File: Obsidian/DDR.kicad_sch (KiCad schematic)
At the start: 59 parts, among them U2 MT41K512M16HA-125_E / MT41K51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

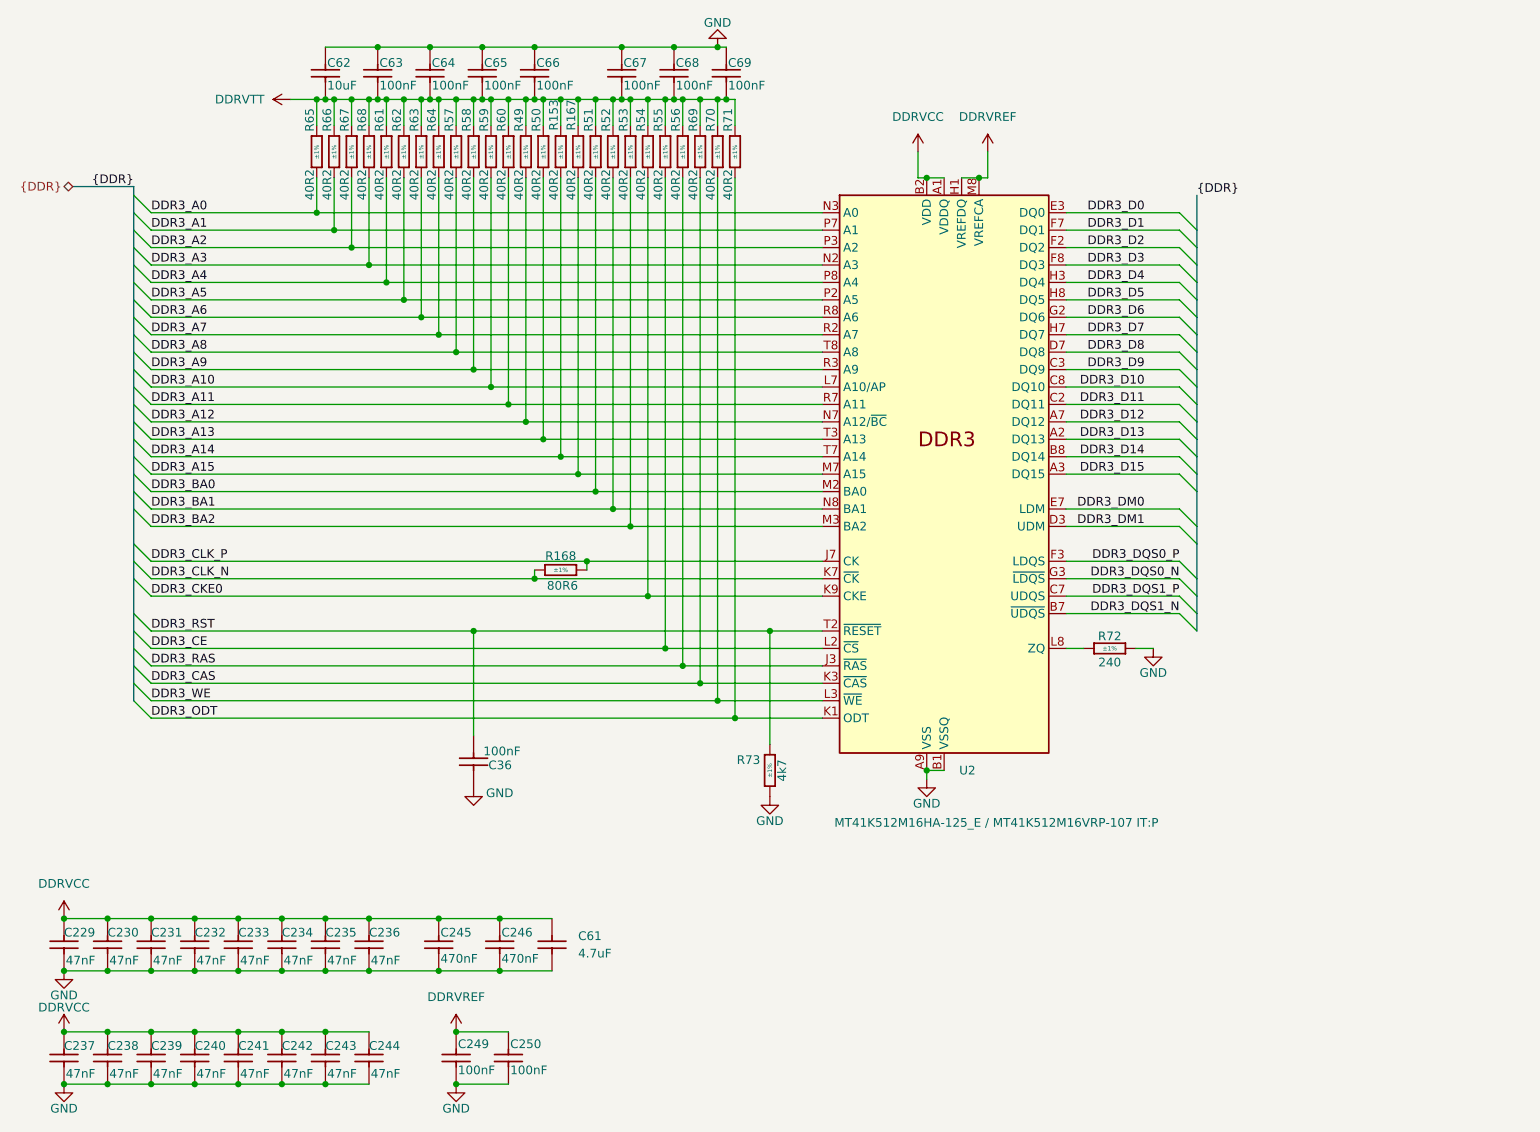
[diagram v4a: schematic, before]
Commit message: Cleaning symbol fields
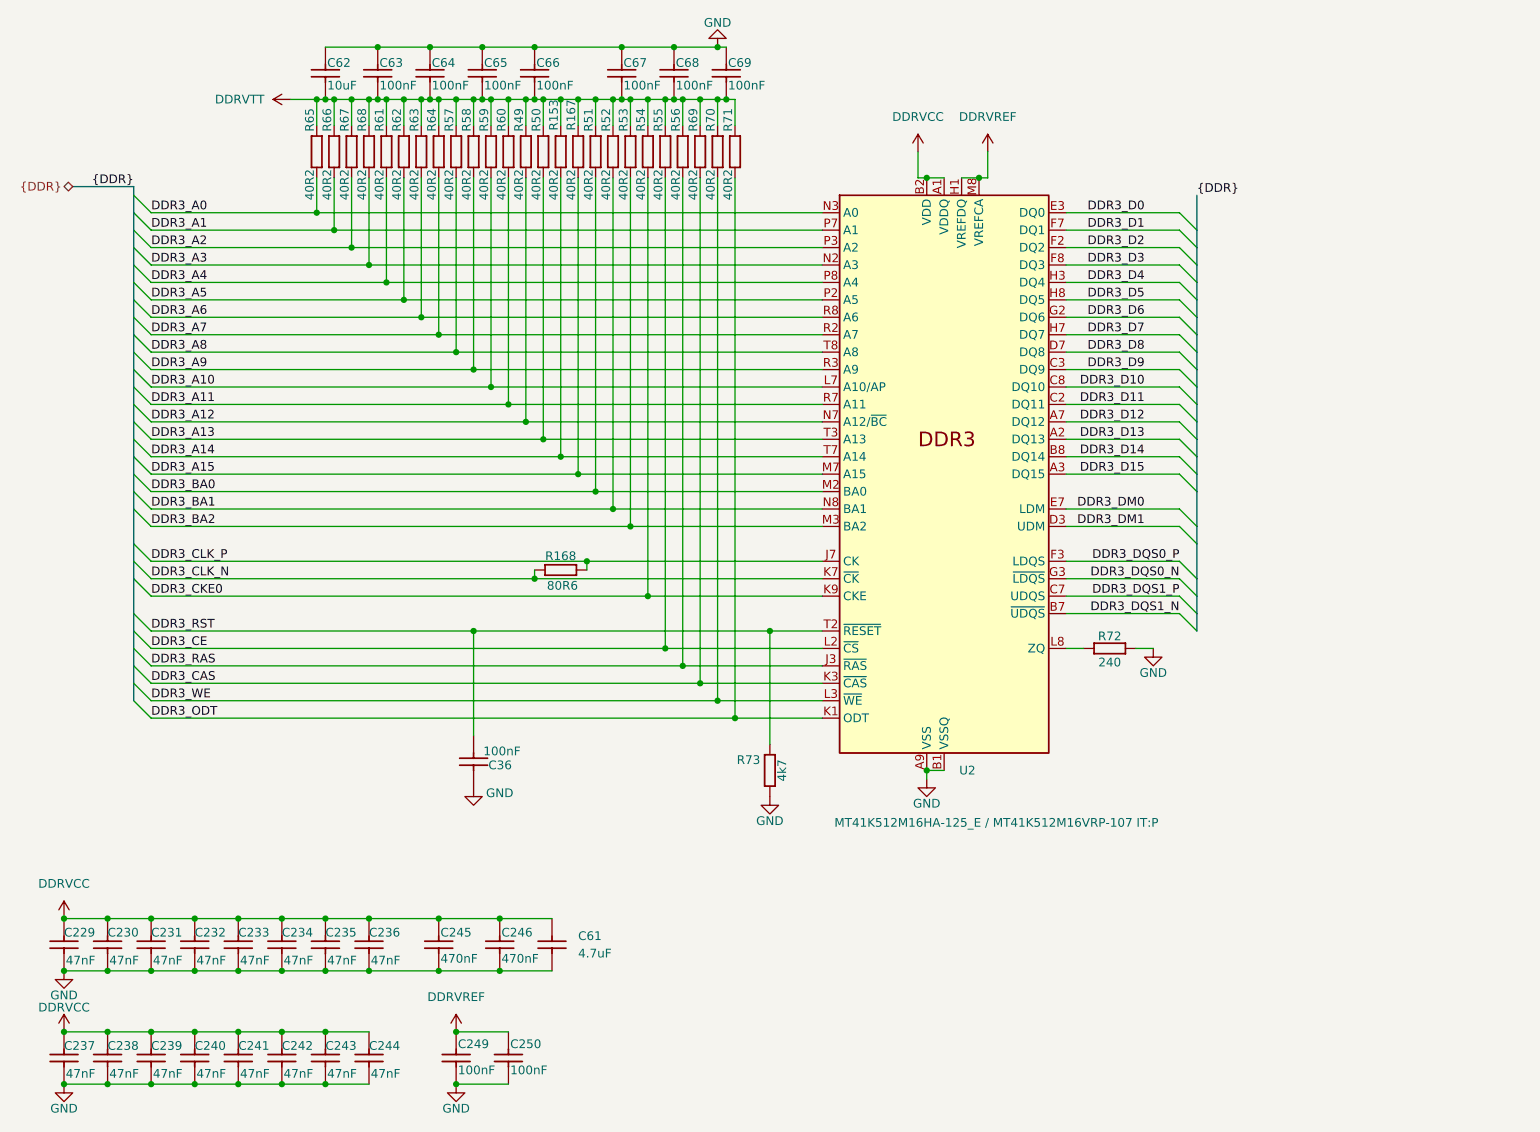
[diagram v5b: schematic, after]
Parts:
- C229, C230, C231, C232, C233, C234, C235, C236, C237, C238, C239, C240, C241, C242, C243, C244: Author CERN DEM JLC -> (none); Case 0201 -> (none); Comment 47nF -> (none); Component Kind Standard -> (none); Component Type Standard -> (none); ComponentHeight (none) -> (none); CreateDate 12/03/07 00:00:00 -> (none); Database Table Name Capacitors -> (none); Footprint Library Capacitors SMD -> (none); Footprint Path PcbLib\Capacitors SMD.PcbLib -> (none); Footprint Ref CAPC0603X33N -> (none); HelpURL \\cern.ch\dfs\Applications\Altium\Datasheets\CC0201_X5R_AVX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 -> (none); LatestRevisionDate 12/03/07 00:00:00 -> (none); Library Name Capacitors SMD -> (none); Library Path SchLib\Capacitors.SchLib -> (none); Library Ref Capacitor - non polarized -> (none); License CC-BY-SA 4.0 -> (none); Manufacturer GENERIC -> (none); Manufacturer Part Number CC0201_47NF_6.3V_10%_X5R -> (none); Manufacturer1 ComponentHeight 0.33mm -> (none); Manufacturer1 Example AVX -> (none); Manufacturer1 Part Number 02016D473KAT2A -> (none); Mounted Yes -> (none); PackageDescription (none) -> (none); Part Description SMD Multilayer Chip Ceramic Capacitor -> (none); Part Number CC0201_47NF_6.3V_10%_X5R -> (none); Pin Count 2 -> (none); PressFit (none) -> (none); SMD Yes -> (none); Sense No -> (none); Sense Comment (none) -> (none); Socket No -> (none); Status Not Recommended -> (none); Status Comment (none) -> (none); TC X5R -> (none); Tolerance ±10% -> (none); Voltage 6.3V -> (none)
- C245, C246: Author CERN DEM JLC -> (none); Case 0201 -> (none); Comment 470nF -> (none); Component Kind Standard -> (none); Component Type Standard -> (none); ComponentHeight (none) -> (none); CreateDate 05/27/10 00:00:00 -> (none); Database Table Name Capacitors -> (none); Footprint Library Capacitors SMD -> (none); Footprint Path PcbLib\Capacitors SMD.PcbLib -> (none); Footprint Ref CAPC0603X33N -> (none); HelpURL \\cern.ch\dfs\Applications\Altium\Datasheets\CC0201_X5R_TAI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 -> (none); LatestRevisionDate 05/27/10 00:00:00 -> (none); Library Name Capacitors SMD -> (none); Library Path SchLib\Capacitors.SchLib -> (none); Library Ref Capacitor - non polarized -> (none); License CC-BY-SA 4.0 -> (none); Manufacturer GENERIC -> (none); Manufacturer Part Number CC0201_470NF_4V_20%_X5R -> (none); Manufacturer1 ComponentHeight 0.33mm -> (none); Manufacturer1 Example TAIYO YUDEN -> (none); Manufacturer1 Part Number AMK063BJ474MP-F -> (none); Mounted Yes -> (none); PackageDescription (none) -> (none); Part Description SMD Multilayer Chip Ceramic Capacitor -> (none); Part Number CC0201_470NF_4V_20%_X5R -> (none); Pin Count 2 -> (none); PressFit (none) -> (none); SMD Yes -> (none); Sense No -> (none); Sense Comment (none) -> (none); Socket No -> (none); Status Not Recommended -> (none); Status Comment (none) -> (none); TC X5R -> (none); Tolerance ±20% -> (none); Voltage 4V -> (none)
- C249, C250: Author CERN DEM JLC -> (none); Case 0201 -> (none); Comment 100nF -> (none); Component Kind Standard -> (none); Component Type Standard -> (none); ComponentHeight (none) -> (none); CreateDate 12/03/07 00:00:00 -> (none); Database Table Name Capacitors -> (none); Footprint Library Capacitors SMD -> (none); Footprint Path PcbLib\Capacitors SMD.PcbLib -> (none); Footprint Ref CAPC0603X33N -> (none); HelpURL \\cern.ch\dfs\Applications\Altium\Datasheets\CC0201_X5R_AVX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 -> (none); LatestRevisionDate 12/03/07 00:00:00 -> (none); Library Name Capacitors SMD -> (none); Library Path SchLib\Capacitors.SchLib -> (none); Library Ref Capacitor - non polarized -> (none); License CC-BY-SA 4.0 -> (none); Manufacturer GENERIC -> (none); Manufacturer Part Number CC0201_100NF_6.3V_10%_X5R -> (none); Manufacturer1 ComponentHeight 0.33mm -> (none); Manufacturer1 Example AVX -> (none); Manufacturer1 Part Number 02016D104KAT2A -> (none); Mounted Yes -> (none); PackageDescription (none) -> (none); Part Description SMD Multilayer Chip Ceramic Capacitor -> (none); Part Number CC0201_100NF_6.3V_10%_X5R -> (none); Pin Count 2 -> (none); PressFit (none) -> (none); SMD Yes -> (none); Sense No -> (none); Sense Comment (none) -> (none); Socket No -> (none); Status Not Recommended -> (none); Status Comment (none) -> (none); TC X5R -> (none); Tolerance ±10% -> (none); Voltage 6.3V -> (none)
- C36, C63, C64, C65, C66, C67, C68, C69: Author CERN DEM MR -> (none); Case 0402 -> (none); Comment 100nF -> (none); Component Kind Standard -> (none); Component Type Standard -> (none); ComponentHeight (none) -> (none); CreateDate 06/30/17 00:00:00 -> (none); Database Table Name Capacitors -> (none); Footprint Library Capacitors SMD -> (none); Footprint Path PcbLib\Capacitors SMD.PcbLib -> (none); Footprint Ref CAPC1005X55N -> (none); HelpURL \\cern.ch\dfs\Applications\Altium\Datasheets\CC0402_MURATA_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 -> (none); LatestRevisionDate 06/30/17 00:00:00 -> (none); Library Name Capacitors SMD -> (none); Library Path SchLib\Capacitors.SchLib -> (none); Library Ref Capacitor - non polarized -> (none); License CC-BY-SA 4.0 -> (none); Manufacturer GENERIC -> (none); Manufacturer Part Number CC0402_100NF_50V_10%_X7R -> (none); Manufacturer1 ComponentHeight 0.55mm -> (none); Manufacturer1 Example MURATA -> (none); Manufacturer1 Part Number GRM155R71H104KE14D -> (none); Mounted Yes -> (none); PackageDescription (none) -> (none); Part Description SMD Multilayer Chip Ceramic Capacitor -> (none); Part Number CC0402_100NF_50V_10%_X7R -> (none); Pin Count 2 -> (none); PressFit (none) -> (none); SMD Yes -> (none); Sense No -> (none); Sense Comment (none) -> (none); Socket No -> (none); Status None -> (none); Status Comment (none) -> (none); TC X7R -> (none); Tolerance ±10% -> (none); Voltage 50V -> (none)
- C61: Author CERN DEM BC -> (none); Case 0402 -> (none); Comment 4.7uF -> (none); Component Kind Standard -> (none); Component Type Standard -> (none); ComponentHeight (none) -> (none); CreateDate 09/07/20 00:00:00 -> (none); Database Table Name Capacitors -> (none); Footprint Library Capacitors SMD -> (none); Footprint Path PcbLib\Capacitors SMD.PcbLib -> (none); Footprint Ref CAPC1005X55N -> (none); HelpURL \\cern.ch\dfs\Applications\Altium\Datasheets\CC0402_X5R_YAG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 -> (none); LatestRevisionDate 09/07/20 00:00:00 -> (none); Library Name Capacitors SMD -> (none); Library Path SchLib\Capacitors.SchLib -> (none); Library Ref Capacitor - non polarized -> (none); License CC-BY-SA 4.0 -> (none); Manufacturer GENERIC -> (none); Manufacturer Part Number CC0402_4.7UF_16V_20%_X5R -> (none); Manufacturer1 ComponentHeight 0.55mm -> (none); Manufacturer1 Example YAGEO PHYCOMP -> (none); Manufacturer1 Part Number CC0402MRX5R7BB475 -> (none); Mounted Yes -> (none); PackageDescription (none) -> (none); Part Description SMD Multilayer Chip Ceramic Capacitor -> (none); Part Number CC0402_4.7UF_16V_20%_X5R -> (none); Pin Count 2 -> (none); PressFit (none) -> (none); SMD Yes -> (none); Sense No -> (none); Sense Comment (none) -> (none); Socket No -> (none); Status Preferred -> (none); Status Comment (none) -> (none); TC X5R -> (none); Tolerance ±20% -> (none); Voltage 16V -> (none)
- C62: Author CERN DEM JLC -> (none); Case 0402 -> (none); Comment 10uF -> (none); Component Kind Standard -> (none); Component Type Standard -> (none); ComponentHeight (none) -> (none); CreateDate 01/07/15 00:00:00 -> (none); Database Table Name Capacitors -> (none); Footprint Library Capacitors SMD -> (none); Footprint Path PcbLib\Capacitors SMD.PcbLib -> (none); Footprint Ref CAPC1005X70N -> (none); HelpURL \\cern.ch\dfs\Applications\Altium\Datasheets\CC0402_X5R_TDK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 -> (none); LatestRevisionDate 01/07/15 00:00:00 -> (none); Library Name Capacitors SMD -> (none); Library Path SchLib\Capacitors.SchLib -> (none); Library Ref Capacitor - non polarized -> (none); License CC-BY-SA 4.0 -> (none); Manufacturer GENERIC -> (none); Manufacturer Part Number CC0402_10UF_6.3V_20%_X5R -> (none); Manufacturer1 ComponentHeight 0.70mm -> (none); Manufacturer1 Example TDK -> (none); Manufacturer1 Part Number C1005X5R0J106M050 -> (none); Mounted Yes -> (none); PackageDescription (none) -> (none); Part Description SMD Multilayer Chip Ceramic Capacitor -> (none); Part Number CC0402_10UF_6.3V_20%_X5R -> (none); Pin Count 2 -> (none); PressFit (none) -> (none); SMD Yes -> (none); Sense No -> (none); Sense Comment (none) -> (none); Socket No -> (none); Status Preferred -> (none); Status Comment (none) -> (none); TC X5R -> (none); Tolerance ±10% -> (none); Voltage 6.3V -> (none)
- R153, R167, R49, R50, R51, R52, R53, R54, R55, R56, R57, R58, R59, R60, R61, R62, R63, R64, R65, R66, R67, R68, R69, R70, R71: Author CERN DEM JLC -> (none); Case 0402 -> (none); Comment 40R2 -> (none); Component Kind Standard -> (none); Component Type Standard -> (none); ComponentHeight (none) -> (none); CreateDate 02/03/15 00:00:00 -> (none); Database Table Name Resistors -> (none); Footprint Library Resistors SMD -> (none); Footprint Path PcbLib\Resistors SMD.PcbLib -> (none); Footprint Ref RESC1005X40N -> (none); HelpURL \\cern.ch\dfs\Applications\Altium\Datasheets\R0402_VISHAY_C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 -> (none); LatestRevisionDate 02/03/15 00:00:00 -> (none); Library Name Resistors SMD -> (none); Library Path SchLib\Resistors.SchLib -> (none); Library Ref Resistor - 1% -> (none); License CC-BY-SA 4.0 -> (none); Manufacturer GENERIC -> (none); Manufacturer Part Number R0402_40R2_1%_0.0625W_100PPM -> (none); Manufacturer1 ComponentHeight 0.4mm -> (none); Manufacturer1 Example VISHAY -> (none); Manufacturer1 Part Number CRCW040240R2FK -> (none); Mounted Yes -> (none); PackageDescription (none) -> (none); Part Description General Purpose Thick Film Chip Resistor -> (none); Part Number R0402_40R2_1%_0.0625W_100PPM -> (none); Pin Count 2 -> (none); Power 0.0625W -> (none); PressFit No -> (none); SMD Yes -> (none); Sense No -> (none); Sense Comment (none) -> (none); Socket No -> (none); Status None -> (none); Status Comment (none) -> (none); TC ±100ppm/°C -> (none); Tolerance ±1% -> (none); Voltage (none) -> (none)
- R168: Author CERN DEM JLC -> (none); Case 0402 -> (none); Comment 80R6 -> (none); Component Kind Standard -> (none); Component Type Standard -> (none); ComponentHeight (none) -> (none); CreateDate 03/03/15 00:00:00 -> (none); Database Table Name Resistors -> (none); Footprint Library Resistors SMD -> (none); Footprint Path PcbLib\Resistors SMD.PcbLib -> (none); Footprint Ref RESC1005X40N -> (none); HelpURL \\cern.ch\dfs\Applications\Altium\Datasheets\R0402_PANASONI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 -> (none); LatestRevisionDate 03/03/15 00:00:00 -> (none); Library Name Resistors SMD -> (none); Library Path SchLib\Resistors.SchLib -> (none); Library Ref Resistor - 1% -> (none); License CC-BY-SA 4.0 -> (none); Manufacturer GENERIC -> (none); Manufacturer Part Number R0402_80R6_1%_0.1W_100PPM -> (none); Manufacturer1 ComponentHeight 0.4mm -> (none); Manufacturer1 Example PANASONIC -> (none); Manufacturer1 Part Number ERJ2RKF80R6X -> (none); Mounted Yes -> (none); PackageDescription (none) -> (none); Part Description General Purpose Thick Film Chip Resistor -> (none); Part Number R0402_80R6_1%_0.1W_100PPM -> (none); Pin Count 2 -> (none); Power 0.1W -> (none); PressFit No -> (none); SMD Yes -> (none); Sense No -> (none); Sense Comment (none) -> (none); Socket No -> (none); Status Not Recommended -> (none); Status Comment (none) -> (none); TC ±100ppm/°C -> (none); Tolerance ±1% -> (none); Voltage 50V -> (none)
- R72: Author CERN DEM JLC -> (none); Case 0402 -> (none); Comment 240 -> (none); Component Kind Standard -> (none); Component Type Standard -> (none); ComponentHeight (none) -> (none); CreateDate 12/03/07 00:00:00 -> (none); Database Table Name Resistors -> (none); Footprint Library Resistors SMD -> (none); Footprint Path PcbLib\Resistors SMD.PcbLib -> (none); Footprint Ref RESC1005X40N -> (none); HelpURL \\cern.ch\dfs\Applications\Altium\Datasheets\R0402_Phycomp_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 -> (none); LatestRevisionDate 10/17/12 00:00:00 -> (none); Library Name Resistors SMD -> (none); Library Path SchLib\Resistors.SchLib -> (none); Library Ref Resistor - 1% -> (none); License CC-BY-SA 4.0 -> (none); Manufacturer GENERIC -> (none); Manufacturer Part Number R0402_240R_1%_0.0625W_100PPM -> (none); Manufacturer1 ComponentHeight 0.4mm -> (none); Manufacturer1 Example YAGEO PHYCOMP -> (none); Manufacturer1 Part Number 232270672401L -> (none); Mounted Yes -> (none); PackageDescription (none) -> (none); Part Description General Purpose Thick Film Chip Resistor -> (none); Part Number R0402_240R_1%_0.0625W_100PPM -> (none); Pin Count 2 -> (none); Power 0.0625W -> (none); PressFit No -> (none); SMD Yes -> (none); Sense No -> (none); Sense Comment (none) -> (none); Socket No -> (none); Status Not Recommended -> (none); Status Comment (none) -> (none); TC ±100ppm/°C -> (none); Tolerance ±1% -> (none); Voltage (none) -> (none)
- R73: Author CERN DEM JLC -> (none); Case 0402 -> (none); Comment 4k7 -> (none); Component Kind Standard -> (none); Component Type Standard -> (none); ComponentHeight (none) -> (none); CreateDate 12/03/07 00:00:00 -> (none); Database Table Name Resistors -> (none); Footprint Library Resistors SMD -> (none); Footprint Path PcbLib\Resistors SMD.PcbLib -> (none); Footprint Ref RESC1005X40N -> (none); HelpURL \\cern.ch\dfs\Applications\Altium\Datasheets\R0402_Phycomp_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 -> (none); LatestRevisionDate 10/17/12 00:00:00 -> (none); Library Name Resistors SMD -> (none); Library Path SchLib\Resistors.SchLib -> (none); Library Ref Resistor - 1% -> (none); License CC-BY-SA 4.0 -> (none); Manufacturer GENERIC -> (none); Manufacturer Part Number R0402_4K7_1%_0.0625W_100PPM -> (none); Manufacturer1 ComponentHeight 0.4mm -> (none); Manufacturer1 Example YAGEO PHYCOMP -> (none); Manufacturer1 Part Number 232270674702L -> (none); Mounted Yes -> (none); PackageDescription (none) -> (none); Part Description General Purpose Thick Film Chip Resistor -> (none); Part Number R0402_4K7_1%_0.0625W_100PPM -> (none); Pin Count 2 -> (none); Power 0.0625W -> (none); PressFit No -> (none); SMD Yes -> (none); Sense No -> (none); Sense Comment (none) -> (none); Socket No -> (none); Status Not Recommended -> (none); Status Comment (none) -> (none); TC ±100ppm/°C -> (none); Tolerance ±1% -> (none); Voltage (none) -> (none)
